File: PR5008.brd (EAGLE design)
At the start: 70 x 70 mm, 48 parts

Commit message: beginnings of changes
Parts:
- removed C17: 470pf, resistor:C0805
- removed JP1: (no value), SparkFun-Connectors:1X05_LOCK
- added C21: 470pF, resistor:C0603
- added JP2: (no value), SparkFun-Connectors:1X03_LOCK
- moved C2 0.20 mm to (19.0, 58.8)
- moved R1 0.20 mm to (23.3, 58.8)
- moved R10 0.20 mm to (16.8, 58.8)
- moved R2 0.20 mm to (25.5, 58.8)
- moved R3 0.20 mm to (21.1, 58.8)
- moved LID 0.10 mm to (53.1, 8.50)
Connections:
- net GND: now also C21.1, JP2.2; no longer C17.2, JP1.4
- net N$12: now also JP2.1; no longer JP1.3
- net N$22: no longer JP1.1
- net N$29: no longer JP1.2
- net N$34: now also C21.2; no longer C17.1
- net VCC: now also JP2.3; no longer JP1.5
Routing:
- net N$29: track 20.6 -> 5.64 mm
- net N$12: track 30.3 -> 26.6 mm
- net N$22: track 28.1 -> 25.0 mm
- net VCC: track 111.3 -> 114.4 mm

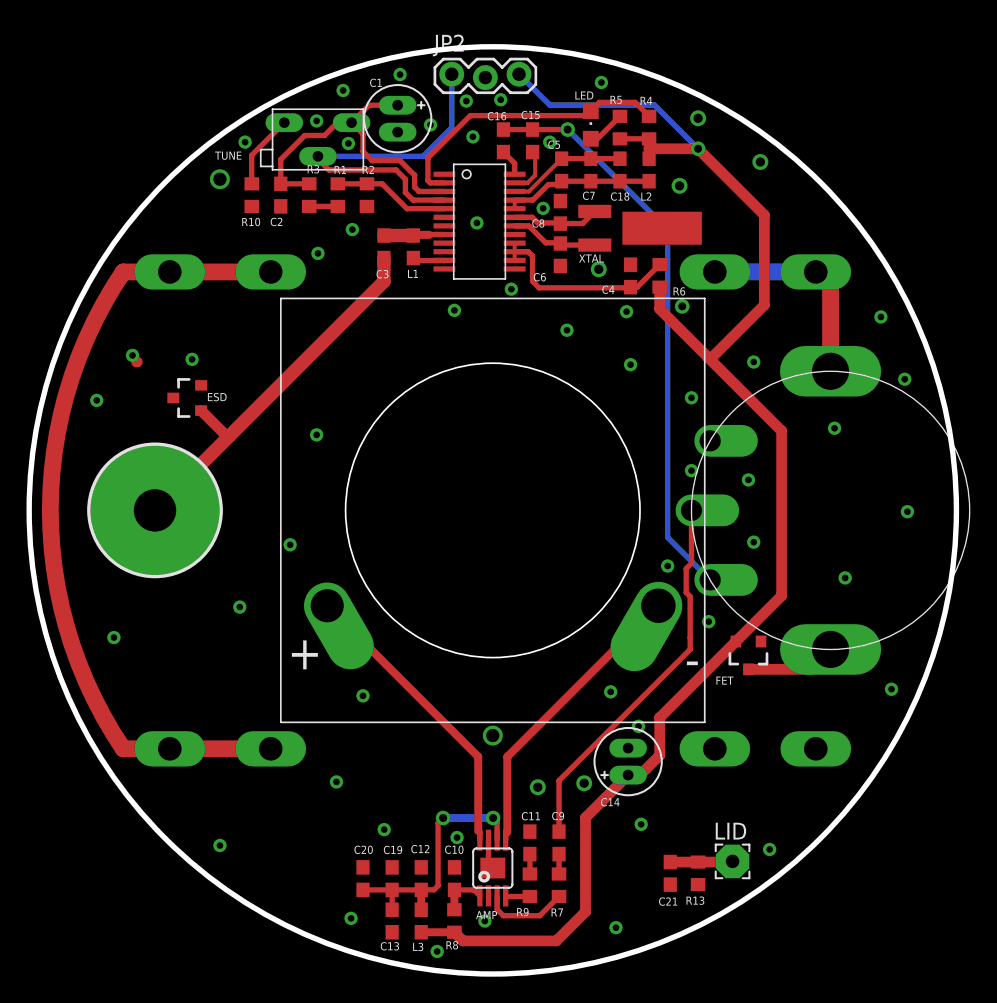
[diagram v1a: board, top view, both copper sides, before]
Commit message: sch update + reset pin screwup
major update to the sch - cleaned it up significantly
also fixed screwup at the reset pin, which was a bug in pr5007
some small brd changes too, mostly around the trimpot
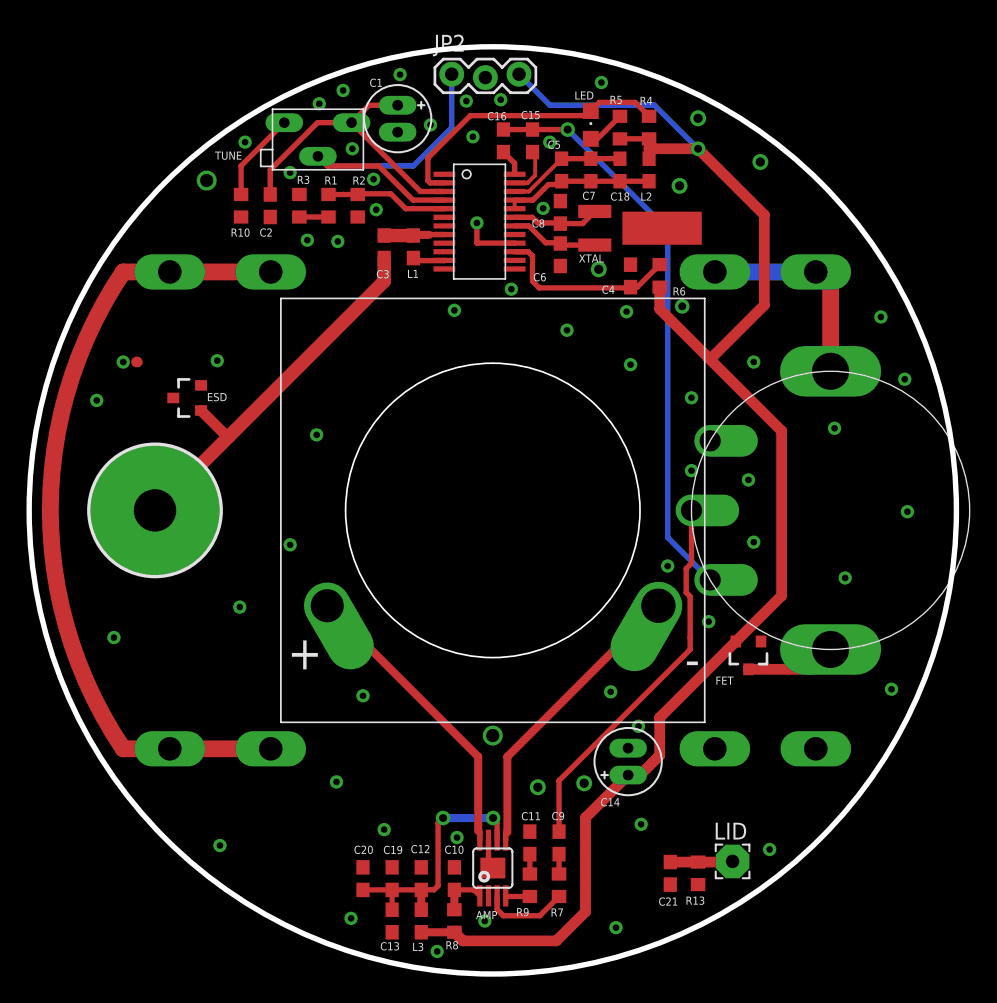
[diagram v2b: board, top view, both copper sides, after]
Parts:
- L2: value 2.5 kOhm @ 100MHz -> 2.5k@100MHz
- TUNE: value TUNE -> 10k
- moved R10 1.13 mm to (16.0, 58.0)
- moved C2 1.13 mm to (18.2, 58.0)
- moved R3 1.09 mm to (20.4, 58.0)
- moved R1 1.06 mm to (22.6, 58.0)
- moved R2 1.06 mm to (24.8, 58.0)
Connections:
- new net N$35: R3.2
- net N$22: no longer R3.2
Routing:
- net GND: track 6.04 -> 9.12 mm, vias 62 -> 65
- net N$22: track 25.0 -> 22.8 mm
- net N$29: track 5.64 -> 6.77 mm

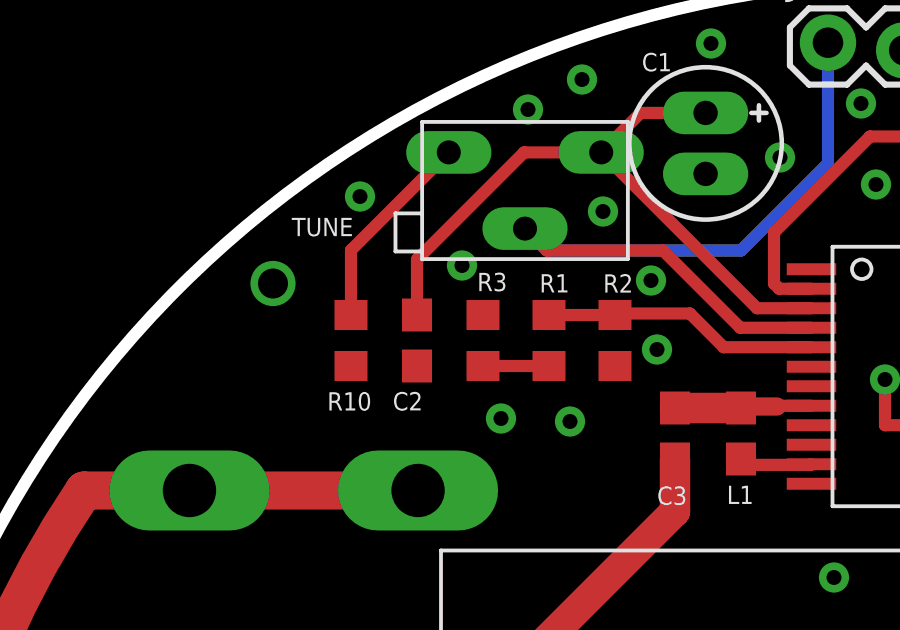
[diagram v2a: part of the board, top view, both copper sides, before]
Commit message: Updates and Fixes
Small changes, clearing Osh Park design rules
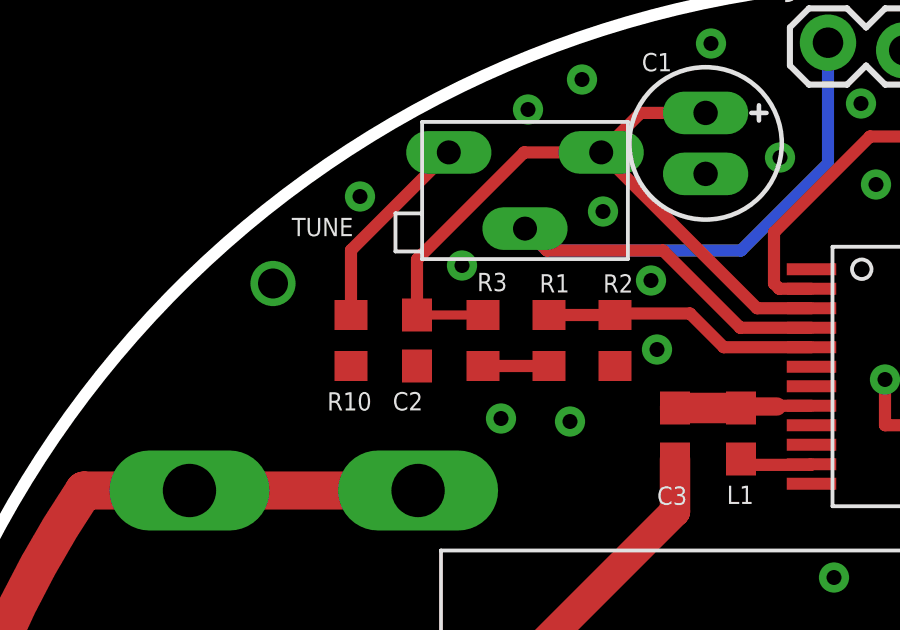
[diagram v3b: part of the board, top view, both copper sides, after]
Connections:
- removed net N$35: R3.2
- net N$22: now also R3.2
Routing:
- net N$22: track 22.8 -> 25.0 mm
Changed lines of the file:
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@@
 <?xml version="1.0" encoding="utf-8"?>
 <!DOCTYPE eagle SYSTEM "eagle.dtd">
-<eagle version="6.6.0">
+<eagle version="6.4">
 <drawing>
 <settings>
@@
 <wire x1="21.77" y1="64.27" x2="18.2" y2="60.7" width="0.4064" layer="1"/>
 <wire x1="18.2" y1="60.7" x2="18.2" y2="58.85" width="0.4064" layer="1"/>
+<contactref element="R3" pad="2"/>
+<wire x1="18.2" y1="58.85" x2="20.4" y2="58.85" width="0.3048" layer="1"/>
 </signal>
 <signal name="N$31">
@@
 <wire x1="59" y1="23" x2="54.3" y2="23" width="0.8128" layer="1"/>
 </signal>
-<signal name="N$35">
-<contactref element="R3" pad="2"/>
-</signal>
 <signal name="N$32">
